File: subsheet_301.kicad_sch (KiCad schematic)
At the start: 19 parts, among them J301 DB-19S ACSI Port, U302 74LS245_PHY, U306 74LS74_PHY, U307 74LS244_PHY

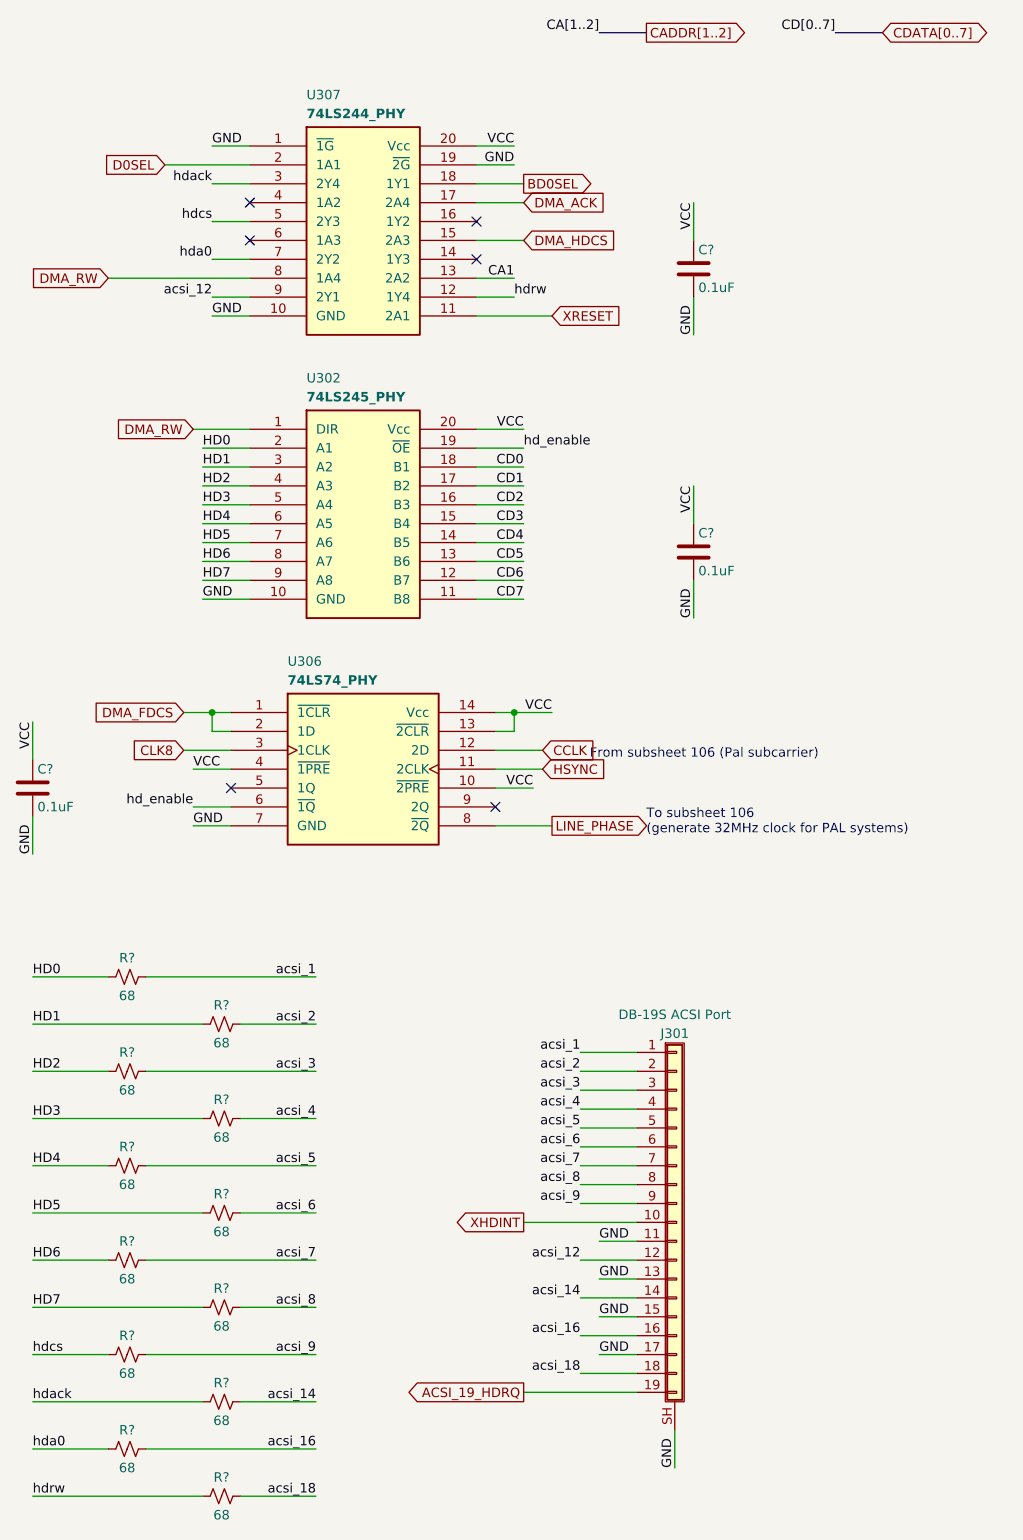
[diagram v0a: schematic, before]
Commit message: Resolves #3 : [schematic] annotate video port with signal name
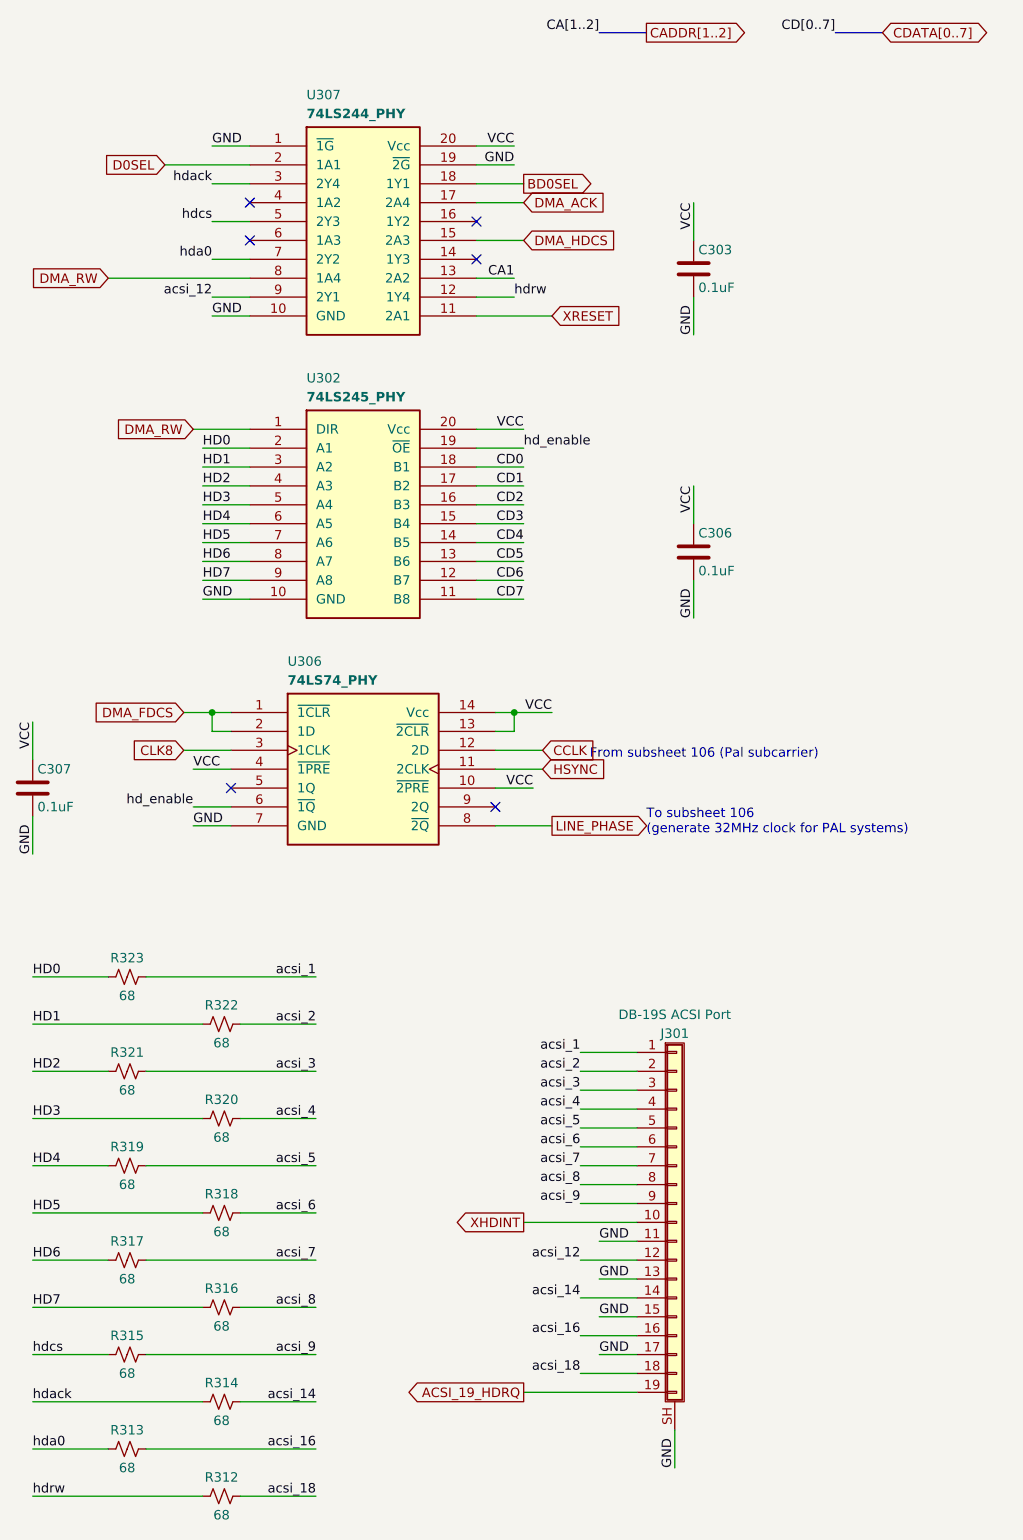
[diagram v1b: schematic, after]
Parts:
- gave numbers to parts that had none: 15
